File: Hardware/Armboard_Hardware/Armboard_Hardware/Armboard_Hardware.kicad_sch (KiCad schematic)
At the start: 239 parts, among them J1 RJ45_LED_Shielded, J2 Conn_02x03_Counter_Clockwise, Q1 SI4156DY, Q10 SI4156DY, Q11 SI4156DY, Q12 SI4156DY, Q13 SI4156DY, Q14 SI4156DY, Q15 SI4156DY, Q16 SI4156DY, Q17 SI4156DY, Q18 SI4156DY, Q19 SI4156DY, Q2 SI4156DY, Q20 SI4156DY, Q21 SI4156DY, Q22 SI4156DY, Q23 SI4156DY, Q24 SI4156DY, Q25 SI4156DY, Q26 SI4156DY, Q27 SI4156DY, Q28 SI4156DY, Q29 BSS138, Q3 SI4156DY, Q30 SI4156DY, Q31 SI4156DY, Q32 SI4156DY, Q33 SI4156DY, Q34 SI4156DY, Q35 SI4156DY, Q36 SI4156DY, Q37 SI4156DY, Q38 BSS138, Q4 SI4156DY, Q5 SI4156DY, Q6 SI4156DY, Q7 SI4156DY, Q8 SI4156DY, Q9 SI4156DY, U1 Teensy4.1_DEV-16771, U10 IRS2005S, U11 IRS2005S, U12 IRS2005S, U13 IRS2005S, U14 OKI, U15 IRS2005S, U16 IRS2005S, U17 IRS2005S, U18 IRS2005S, U19 IRS2005S, U2 IRS2005S, U20 IRS2005S, U21 74LVC2G04, U22 74LVC2G04, U23 74LVC2G04, U24 74LVC2G04, U25 74LVC2G04, U26 74LVC2G04, U27 74LVC2G04, U28 74LVC2G04, U29 74LVC2G04, U3 IRS2005S, U4 IRS2005S, U5 IRS2005S, U6 IRS2005S, U7 IRS2005S, U8 IRS2005S, U9 IRS2005S

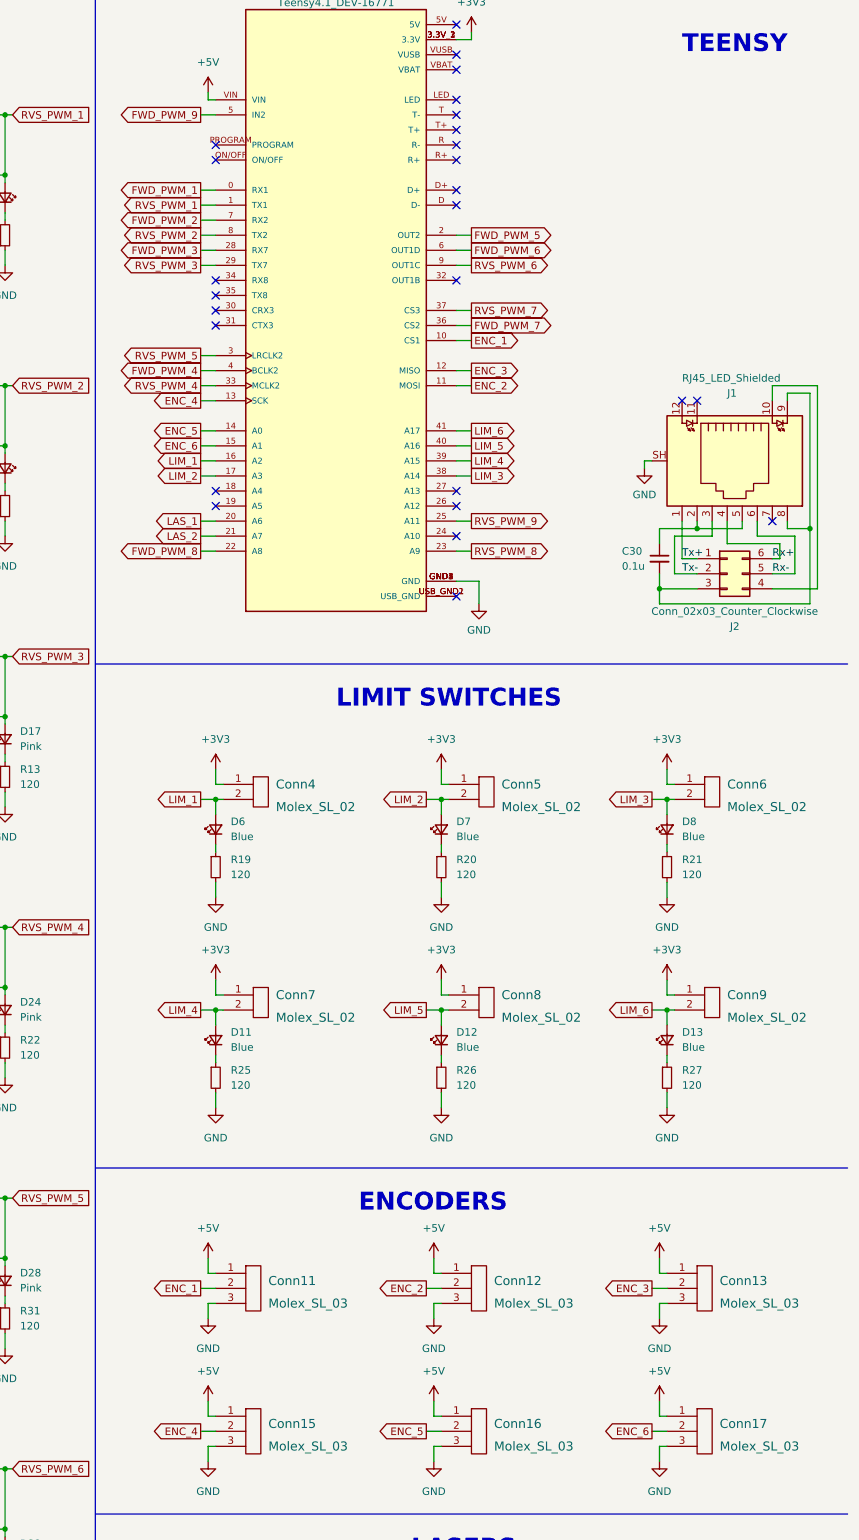
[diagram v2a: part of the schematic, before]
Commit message: Board Shrink + Rerout + Pin Reassignment
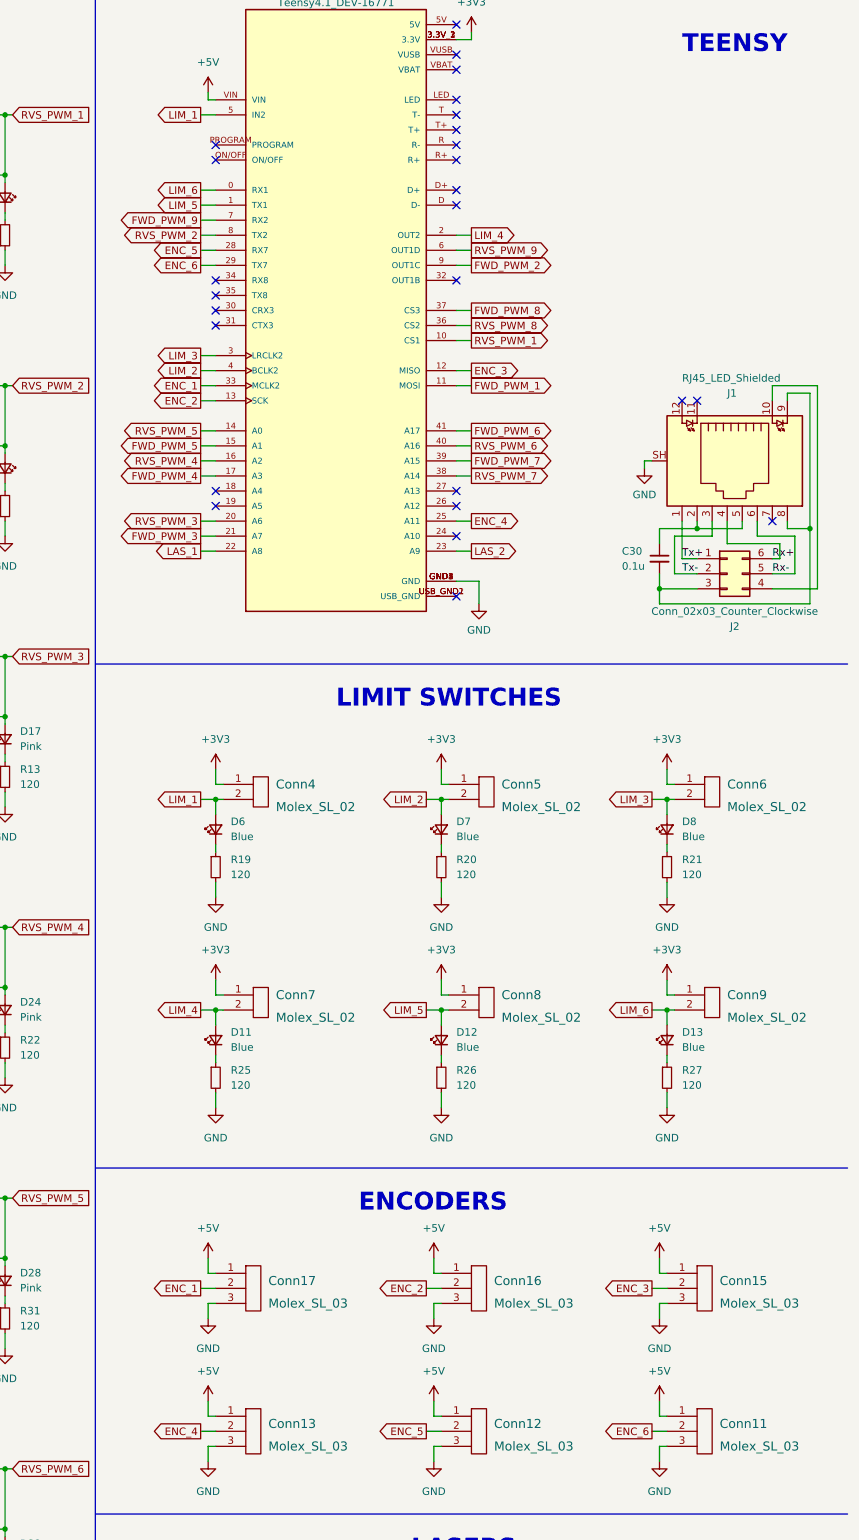
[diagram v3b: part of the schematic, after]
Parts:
- U1: footprint MRDT_Shields:Teensy_4_1 -> MRDT_Shields:Teensy_4_1_Bare
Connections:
- net ENC_1: now also Conn17.2, U1.33 (MCLK2); no longer Conn11.2, U1.10 (CS1)
- net ENC_2: now also Conn16.2, U1.13 (SCK); no longer Conn12.2, U1.11 (MOSI)
- net ENC_3: now also Conn15.2; no longer Conn13.2
- net ENC_4: now also Conn13.2, U1.25 (A11); no longer Conn15.2, U1.13 (SCK)
- net ENC_5: now also Conn12.2, U1.28 (RX7); no longer Conn16.2, U1.14 (A0)
- net ENC_6: now also Conn11.2, U1.29 (TX7); no longer Conn17.2, U1.15 (A1)
- net FWD_PWM_1: now also U1.11 (MOSI); no longer U1.0 (RX1)
- net FWD_PWM_2: now also U1.9 (OUT1C); no longer U1.7 (RX2)
- net FWD_PWM_3: now also U1.21 (A7); no longer U1.28 (RX7)
- net FWD_PWM_4: now also U1.17 (A3); no longer U1.4 (BCLK2)
- net FWD_PWM_5: now also U1.15 (A1); no longer U1.2 (OUT2)
- net FWD_PWM_6: now also U1.41 (A17); no longer U1.6 (OUT1D)
- net FWD_PWM_7: now also U1.39 (A15); no longer U1.36 (CS2)
- net FWD_PWM_8: now also U1.37 (CS3); no longer U1.22 (A8)
- net FWD_PWM_9: now also U1.7 (RX2); no longer U1.5 (IN2)
- net LAS_1: now also U1.22 (A8); no longer U1.20 (A6)
- net LAS_2: now also U1.23 (A9); no longer U1.21 (A7)
- net LIM_1: now also U1.5 (IN2); no longer U1.16 (A2)
- net LIM_2: now also U1.4 (BCLK2); no longer U1.17 (A3)
- net LIM_3: now also U1.3 (LRCLK2); no longer U1.38 (A14)
- net LIM_4: now also U1.2 (OUT2); no longer U1.39 (A15)
- net LIM_5: now also U1.1 (TX1); no longer U1.40 (A16)
- net LIM_6: now also U1.0 (RX1); no longer U1.41 (A17)
- net RVS_PWM_1: now also U1.10 (CS1); no longer U1.1 (TX1)
- net RVS_PWM_3: now also U1.20 (A6); no longer U1.29 (TX7)
- net RVS_PWM_4: now also U1.16 (A2); no longer U1.33 (MCLK2)
- net RVS_PWM_5: now also U1.14 (A0); no longer U1.3 (LRCLK2)
- net RVS_PWM_6: now also U1.40 (A16); no longer U1.9 (OUT1C)
- net RVS_PWM_7: now also U1.38 (A14); no longer U1.37 (CS3)
- net RVS_PWM_8: now also U1.36 (CS2); no longer U1.23 (A9)
- net RVS_PWM_9: now also U1.6 (OUT1D); no longer U1.25 (A11)
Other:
- moved on the sheet: Conn11, Conn12, Conn13, Conn15, Conn16, Conn17

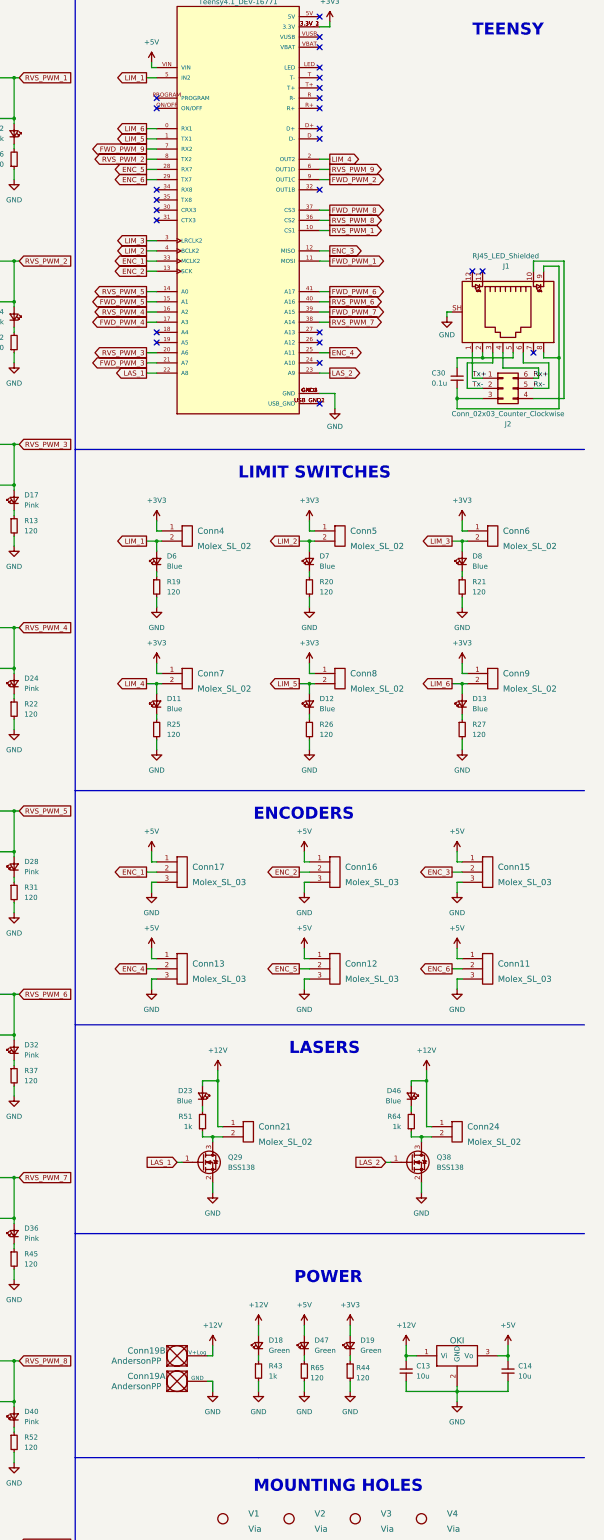
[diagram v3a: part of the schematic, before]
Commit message: Added 6 limit switches
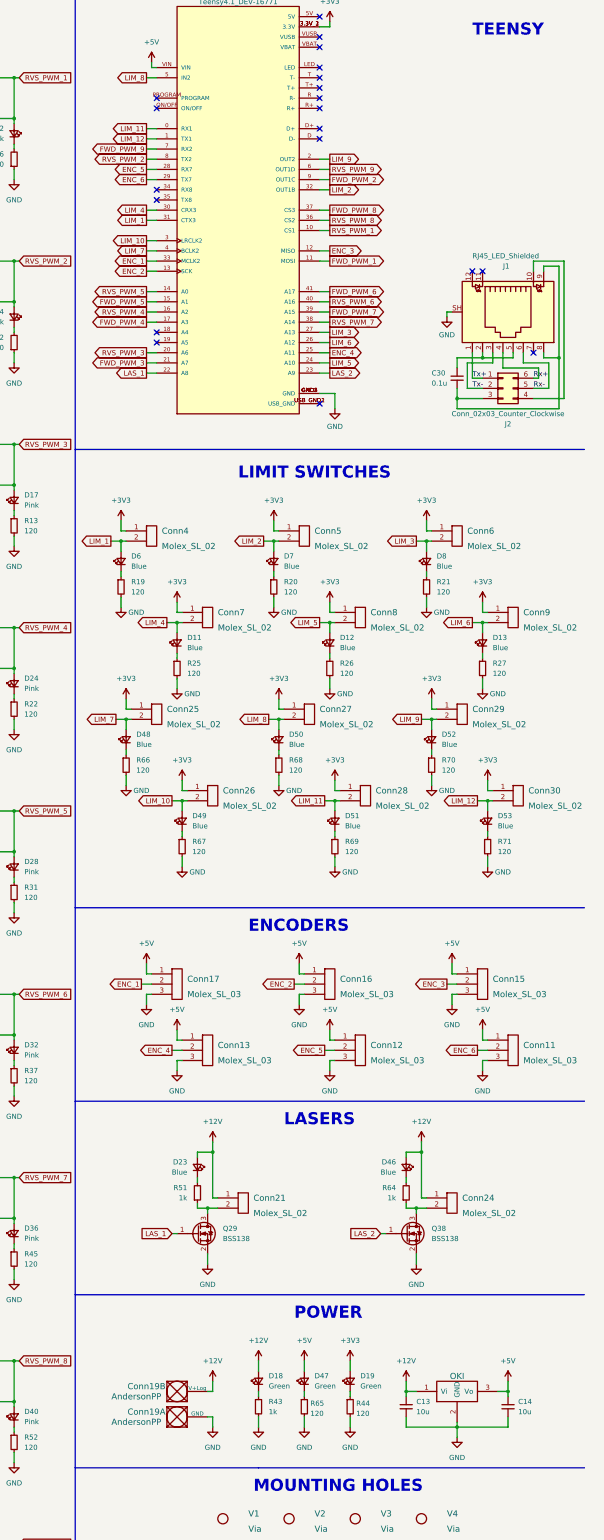
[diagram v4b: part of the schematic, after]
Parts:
- added Conn25, Conn26, Conn27, Conn28, Conn29, Conn30: Molex_SL_02, Connector_Molex:Molex_SL_171971-0002_1x02_P2.54mm_Vertical, symbol MRDT_Connectors:Molex_SL_02
- added D48, D49, D50, D51, D52, D53: Blue, LED_SMD:LED_0603_1608Metric_Pad1.05x0.95mm_HandSolder, symbol Device:LED_Small
- added R66, R67, R68, R69, R70, R71: 120, Resistor_SMD:R_0603_1608Metric_Pad0.98x0.95mm_HandSolder, symbol Device:R_Small
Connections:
- net +3V3: now also Conn25.1, Conn26.1, Conn27.1, Conn28.1, Conn29.1, Conn30.1
- net GND: now also R66.2, R67.2, R68.2, R69.2, R70.2, R71.2
- net LIM_1: now also U1.31 (CTX3); no longer U1.5 (IN2)
- net LIM_2: now also U1.32 (OUT1B); no longer U1.4 (BCLK2)
- net LIM_3: now also U1.27 (A13); no longer U1.3 (LRCLK2)
- net LIM_4: now also U1.30 (CRX3); no longer U1.2 (OUT2)
- net LIM_5: now also U1.24 (A10); no longer U1.1 (TX1)
- net LIM_6: now also U1.26 (A12); no longer U1.0 (RX1)
- new net: D51.1 (K), R69.1
- new net: D49.1 (K), R67.1
- new net: D53.1 (K), R71.1
- new net: D48.1 (K), R66.1
- new net: D52.1 (K), R70.1
- new net: D50.1 (K), R68.1
- new net LIM_10: Conn26.2, D49.2 (A), U1.3 (LRCLK2)
- new net LIM_11: Conn28.2, D51.2 (A), U1.0 (RX1)
- new net LIM_12: Conn30.2, D53.2 (A), U1.1 (TX1)
- new net LIM_7: Conn25.2, D48.2 (A), U1.4 (BCLK2)
- new net LIM_8: Conn27.2, D50.2 (A), U1.5 (IN2)
- new net LIM_9: Conn29.2, D52.2 (A), U1.2 (OUT2)
- no-connect marks 26 -> 20
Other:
- moved on the sheet: C13, C14, Conn11, Conn12, Conn13, Conn15, Conn16, Conn17, Conn19A, Conn19B, Conn21, Conn24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

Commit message: Add buttons and 16:4 priority encoder
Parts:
- added C31: 470uF, Capacitor_THT:CP_Radial_D6.3mm_P2.50mm, symbol Device:C_Small
- added C32: 220uF, Capacitor_THT:CP_Radial_D6.3mm_P2.50mm, symbol Device:C_Small
- added C33: 110uF, Capacitor_THT:CP_Radial_D6.3mm_P2.50mm, symbol Device:C_Small
- added D54, D55, D56, D57, D58, D59, D60, D61, D62, D63, D64, D65, D66, D67: Blue, LED_SMD:LED_0603_1608Metric_Pad1.05x0.95mm_HandSolder, symbol Device:LED_Small
- added R72, R73, R74, R75, R76, R77, R78, R79, R80, R81, R82, R83, R84, R85: 120, Resistor_SMD:R_0603_1608Metric_Pad0.98x0.95mm_HandSolder, symbol Device:R_Small
- added SW1, SW2, SW3, SW4, SW5, SW6, SW7, SW8, SW9: SW_Push_SPDT, symbol Switch:SW_Push_SPDT
- added SW10: SW_SPDT, symbol Switch:SW_SPDT
- added U30, U31: 74HC148, Package_SO:SOIC-16_4.55x10.3mm_P1.27mm, symbol 74xx:74LS148
- added U32: 74HC00, Package_SO:SO-14_5.3x10.2mm_P1.27mm, symbol 74xx:74HC00
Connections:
- net +12V: now also C31.1, C32.1, C33.1
- net +3V3: now also D58.2 (A), D59.2 (A), D60.2 (A), D61.2 (A), D62.2 (A), D63.2 (A), D64.2 (A), D65.2 (A), D66.2 (A), D67.2 (A), SW1.1 (A), SW10.1 (A), SW2.1 (A), SW3.1 (A), SW4.1 (A), SW5.1 (A), SW6.1 (A), SW7.1 (A), SW8.1 (A), SW9.1 (A), U30.1 (I4), U30.12 (I2), U30.13 (I3), U30.16 (VCC), U30.2 (I5), U30.3 (I6), U30.4 (I7), U31.10 (IO), U31.16 (VCC), U32.14 (VCC)
- net ENC_1: now also U1.41 (A17); no longer U1.33 (MCLK2)
- net ENC_2: now also U1.40 (A16); no longer U1.13 (SCK)
- net ENC_3: now also U1.39 (A15); no longer U1.12 (MISO)
- net ENC_4: now also U1.38 (A14); no longer U1.25 (A11)
- net ENC_5: now also U1.27 (A13); no longer U1.28 (RX7)
- net ENC_6: now also U1.26 (A12); no longer U1.29 (TX7)
- net FWD_PWM_1: now also U1.0 (RX1); no longer U1.11 (MOSI)
- net FWD_PWM_2: now also U1.2 (OUT2); no longer U1.9 (OUT1C)
- net FWD_PWM_3: now also U1.7 (RX2); no longer U1.21 (A7)
- net FWD_PWM_4: now also U1.6 (OUT1D); no longer U1.17 (A3)
- net FWD_PWM_5: now also U1.22 (A8); no longer U1.15 (A1)
- net FWD_PWM_6: now also U1.24 (A10); no longer U1.41 (A17)
- net FWD_PWM_7: now also U1.28 (RX7); no longer U1.39 (A15)
- net FWD_PWM_8: now also U1.36 (CS2); no longer U1.37 (CS3)
- net FWD_PWM_9: now also U1.4 (BCLK2); no longer U1.7 (RX2)
- net GND: now also C31.2, C32.2, C33.2, R72.2, R73.2, R74.2, R75.2, SW1.3 (C), SW10.3 (C), SW2.3 (C), SW3.3 (C), SW4.3 (C), SW5.3 (C), SW6.3 (C), SW7.3 (C), SW8.3 (C), SW9.3 (C), U30.5 (EI), U30.8 (GND), U31.8 (GND), U32.7 (GND)
- net LAS_1: now also U1.12 (MISO); no longer U1.22 (A8)
- net LAS_2: now also U1.11 (MOSI); no longer U1.23 (A9)
- net LIM_1: now also U1.14 (A0); no longer U1.31 (CTX3)
- net LIM_10: now also U1.13 (SCK); no longer U1.3 (LRCLK2)
- net LIM_11: now also U1.32 (OUT1B); no longer U1.0 (RX1)
- net LIM_12: no longer U1.1 (TX1)
- net LIM_2: now also U1.15 (A1); no longer U1.32 (OUT1B)
- net LIM_3: now also U1.16 (A2); no longer U1.27 (A13)
- net LIM_4: now also U1.17 (A3); no longer U1.30 (CRX3)
- net LIM_5: now also U1.18 (A4); no longer U1.24 (A10)
- net LIM_6: now also U1.19 (A5); no longer U1.26 (A12)
- net LIM_7: now also U1.20 (A6); no longer U1.4 (BCLK2)
- net LIM_8: now also U1.21 (A7); no longer U1.5 (IN2)
- net LIM_9: now also U1.33 (MCLK2); no longer U1.2 (OUT2)
- net RVS_PWM_1: now also U1.1 (TX1); no longer U1.10 (CS1)
- net RVS_PWM_2: now also U1.3 (LRCLK2); no longer U1.8 (TX2)
- net RVS_PWM_3: now also U1.8 (TX2); no longer U1.20 (A6)
- net RVS_PWM_4: now also U1.9 (OUT1C); no longer U1.16 (A2)
- net RVS_PWM_5: now also U1.23 (A9); no longer U1.14 (A0)
- net RVS_PWM_6: now also U1.25 (A11); no longer U1.40 (A16)
- net RVS_PWM_7: now also U1.29 (TX7); no longer U1.38 (A14)
- net RVS_PWM_8: now also U1.37 (CS3); no longer U1.36 (CS2)
- net RVS_PWM_9: now also U1.5 (IN2); no longer U1.6 (OUT1D)
- net B_ENC_0: now reaches U1.34 (RX8)
- net B_ENC_0: now also D57.2 (A), U32.11
- net B_ENC_1: now reaches U1.35 (TX8)
- net B_ENC_1: now also D56.2 (A), U32.8
- new net: D54.1 (K), R72.1
- new net: D66.1 (K), R84.1
- new net: U30.7 (S1), U32.10
- new net: U31.7 (S1), U32.9
- new net: D57.1 (K), R75.1
- new net: D65.1 (K), R83.1
- new net: D67.1 (K), R85.1
- new net: D64.1 (K), R82.1
- new net: D60.1 (K), R78.1
- new net: D58.1 (K), R76.1
- new net: D61.1 (K), R79.1
- new net: D59.1 (K), R77.1
- new net: U31.14 (GS), U32.1
- new net: U31.6 (S2), U32.4
- new net: U31.9 (S0), U32.12
- new net: D62.1 (K), R80.1
- new net: U30.14 (GS), U32.2
- new net: U30.6 (S2), U32.5
- new net: U30.9 (S0), U32.13
- new net: D56.1 (K), R74.1
- new net: D63.1 (K), R81.1
- new net: D55.1 (K), R73.1
- new net B_1: R76.2, SW1.2 (B), U31.11 (I1)
- new net B_2: R77.2, SW2.2 (B), U31.12 (I2)
- new net B_3: R78.2, SW3.2 (B), U31.13 (I3)
- new net B_4: R79.2, SW4.2 (B), U31.1 (I4)
- new net B_5: R80.2, SW5.2 (B), U31.2 (I5)
- new net B_6: R81.2, SW6.2 (B), U31.3 (I6)
- new net B_7: R82.2, SW7.2 (B), U31.4 (I7)
- new net B_8: R83.2, SW8.2 (B), U30.10 (IO)
- new net B_9: R84.2, SW9.2 (B), U30.11 (I1)
- new net B_ENC_2: D55.2 (A), U1.30 (CRX3), U32.6
- new net B_ENC_3: D54.2 (A), U1.31 (CTX3), U30.15 (EO), U31.5 (EI)
- new net DIR_SW: R85.2, SW10.2 (B), U1.10 (CS1)
- no-connect marks 20 -> 18
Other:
- note added: "BUTTON 16:4 ENCODER"
- note added: "BUTTONS"
- moved on the sheet: C1, C10, C11, C12, C13, C14, C15, C16, C17, C18, C19, C2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
